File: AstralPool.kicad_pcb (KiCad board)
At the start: 2 copper layers, 80 x 75 mm, 25 parts, among them J1 RJ12, J2 RJ12, J3 Header, Q1 2N3904, U1 LM2678T-5.0/NOPB

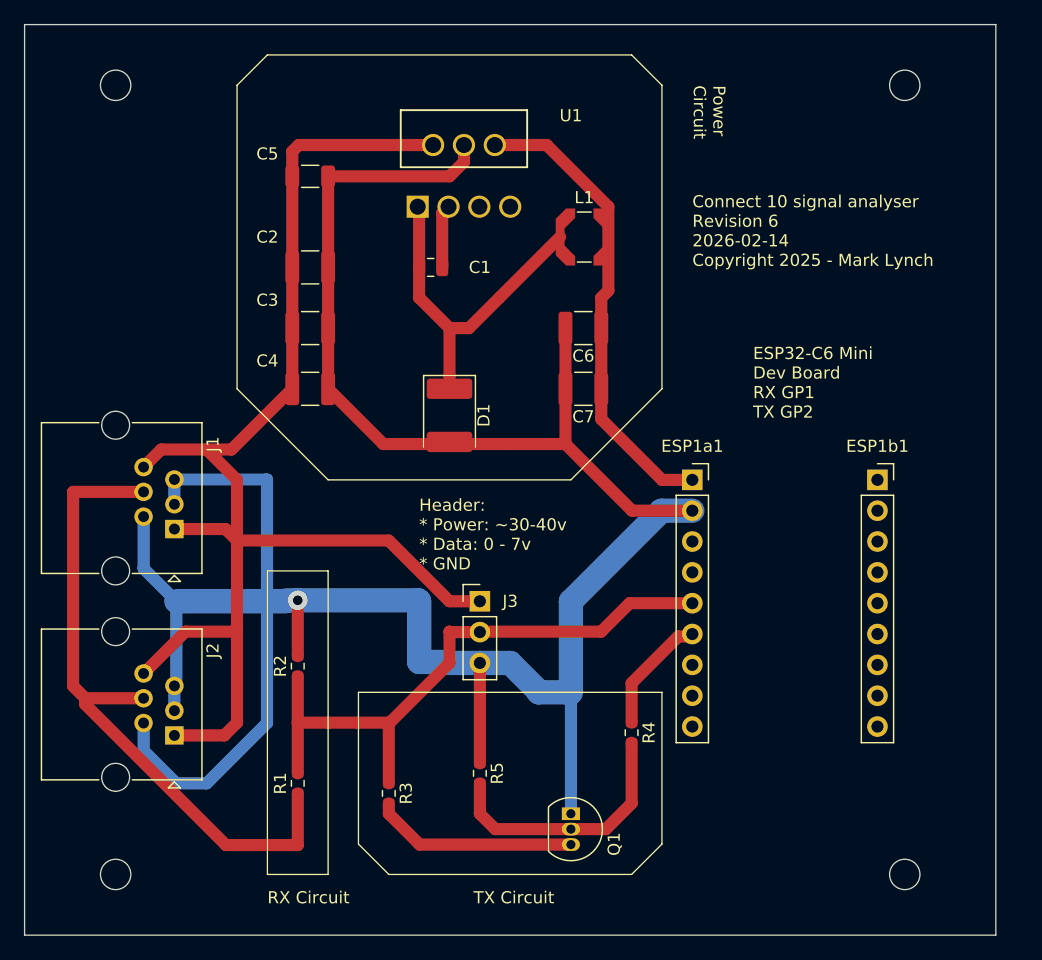
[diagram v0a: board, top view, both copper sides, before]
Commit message: ### Changed - Reorient board to allow all plugs on one side
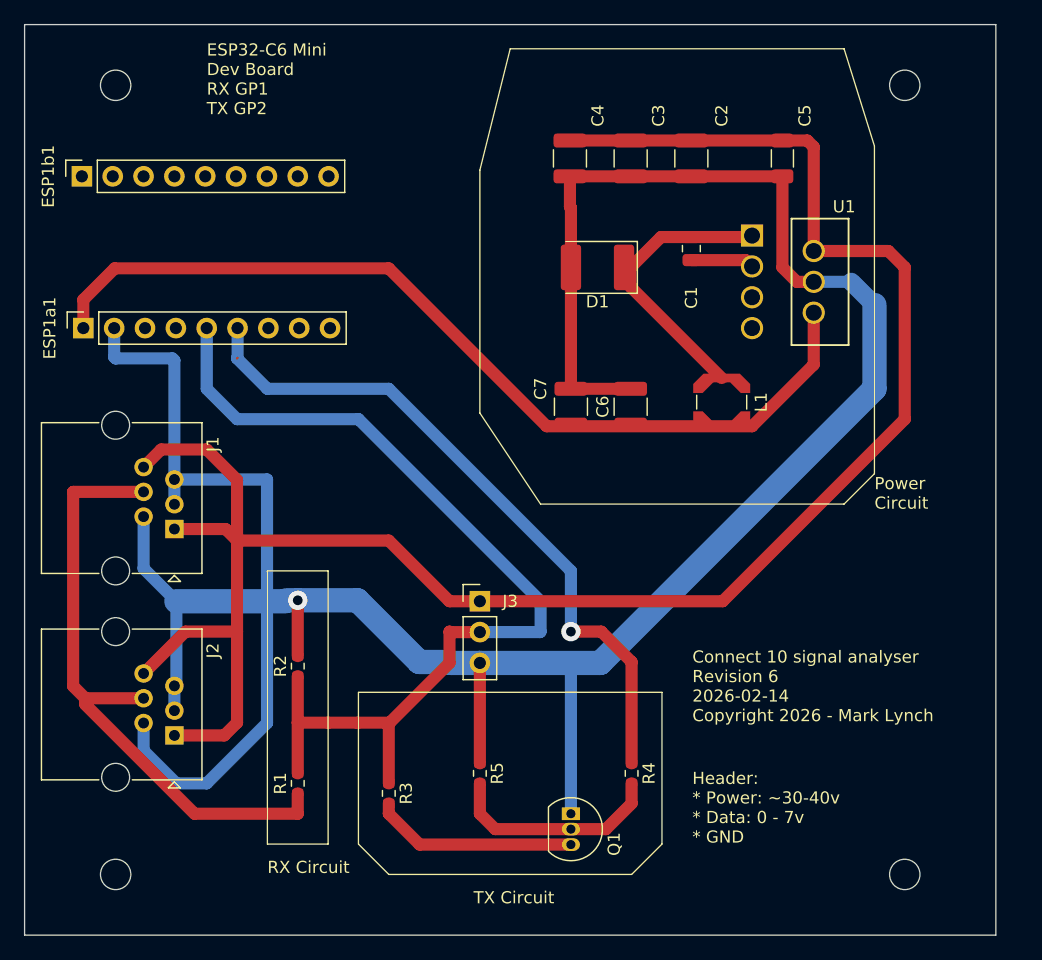
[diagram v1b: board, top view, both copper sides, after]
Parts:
- REF** (x4): value MountingHole_2.5mm -> Mounting 2.5mm
- moved ESP1b1 70.1 mm to (59.7, 35.0), turned to 90 degrees
- moved ESP1a1 51.7 mm to (59.8, 47.5), turned to 90 degrees
- moved C5 38.9 mm to (117.4, 33.5), turned to -90 degrees
- moved U1 37.7 mm to (126.1, 47.5), turned to -90 degrees
- moved C2 32.7 mm to (109.9, 33.5), turned to -90 degrees
- moved C3 29.9 mm to (104.9, 33.5), turned to -90 degrees
- moved C4 28.6 mm to (99.9, 33.5), turned to -90 degrees
- moved C1 21.5 mm to (109.9, 41.0), turned to -90 degrees
- moved L1 17.7 mm to (112.4, 53.6), turned to -90 degrees
- moved D1 17.2 mm to (102.2, 42.5), turned to 180 degrees
- moved C6 7.56 mm to (104.9, 54.0), turned to 90 degrees
- moved R4 3.35 mm to (105.0, 84.2)
- moved C7 1.80 mm to (100.0, 54.0), turned to 90 degrees
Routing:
- net +24V (from connector): track 112.2 -> 162.3 mm
- net Net-(ESP1a1-Pin_6): track 9.93 -> 56.7 mm, vias 0 -> 1
- net +5V (from buck power): track 38.8 -> 75.3 mm
- net Net-(ESP1a1-Pin_5): track 51.2 -> 80.0 mm
- net GND (from connector): track 218.9 -> 237.2 mm
- net Net-(D1-K): track 28.3 -> 23.3 mm
- net Net-(J1-Pad4): track 55.1 -> 51.4 mm
- net Net-(Q1-B): track 21.4 -> 18.1 mm

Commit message: ### Changed - Rev 7 - Reorient power circuit again to make cleaner
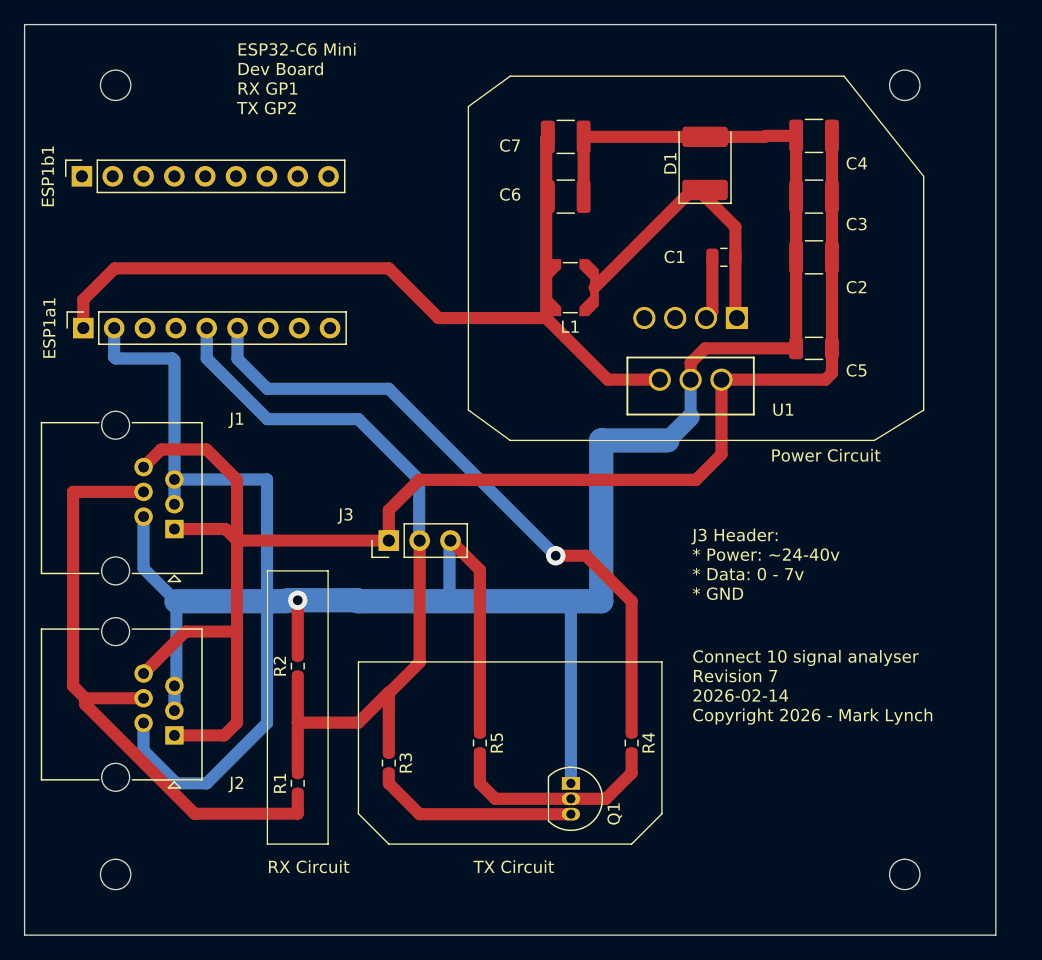
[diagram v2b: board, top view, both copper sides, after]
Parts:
- moved U1 22.6 mm to (106.0, 57.9), turned to 180 degrees
- moved C7 22.2 mm to (99.6, 31.8), turned to 0 degrees
- moved C4 20.2 mm to (120.0, 31.7), turned to 180 degrees
- moved C6 18.1 mm to (99.6, 36.7), turned to 0 degrees
- moved C5 15.9 mm to (120.0, 49.2), turned to 180 degrees
- moved L1 15.6 mm to (100.0, 44.2), turned to 180 degrees
- moved C3 15.4 mm to (120.0, 36.7), turned to 180 degrees
- moved C2 13.0 mm to (120.0, 41.7), turned to 180 degrees
- moved D1 12.3 mm to (111.0, 33.9), turned to 90 degrees
- moved J3 9.01 mm to (85.0, 65.0), turned to 90 degrees
- moved C1 2.78 mm to (112.6, 41.7), turned to 180 degrees
- moved Q1 2.50 mm to (100.0, 85.0)
- moved R3 2.50 mm to (85.0, 83.3)
- moved R4 2.50 mm to (105.0, 81.7)
- moved R5 2.50 mm to (92.5, 81.7)
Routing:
- net +24V (from connector): track 162.3 -> 128.9 mm
- net Net-(ESP1a1-Pin_5): track 80.0 -> 64.3 mm
- net GND (from connector): track 237.2 -> 231.2 mm
- net +5V (from buck power): track 75.3 -> 69.7 mm
- net Net-(ESP1a1-Pin_6): track 56.7 -> 54.1 mm
- net Net-(D1-K): track 23.3 -> 24.1 mm
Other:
- board text added: "J3 Header: * Power: ~24-40v * Data: 0 - 7v * GND"
- board text removed: "Header: * Power: ~30-40v * Data: 0 - 7v * GND"

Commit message: ### Added - Reworked and tested TX circuit
### Changed
- Rev 8 - Updated all footprints to correct specs
- Rev 8 - Updated components to include part numbers
- Rev 8 - Respecced the power circuit based on TI toolins
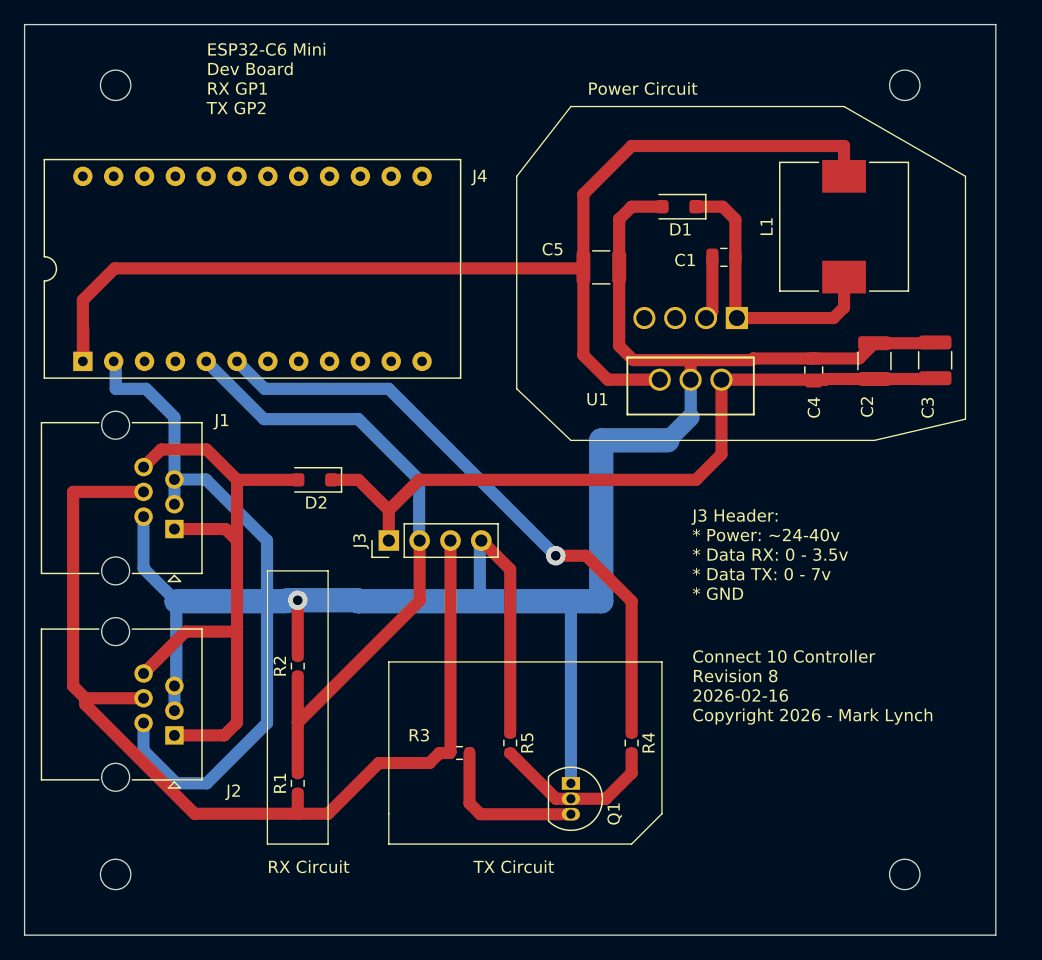
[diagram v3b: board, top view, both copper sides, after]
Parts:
- removed the C4 at (120.0, 31.7)
- removed C7: C 180uF/16v, Capacitor_SMD:C_1210_3225Metric
- removed ESP1a1, ESP1b1: Conn_01x09_Socket, Connector_PinSocket_2.54mm:PinSocket_1x09_P2.54mm_Vertical
- added D2: D 6TQ045S, Diode_SMD:D_SOD-123F, F.Cu at (78.9, 60.0)
- added J4: Conn_02x12_Counter_Clockwise, Package_DIP:DIP-24_18.0mmx34.29mm_W15.24mm_Socket, F.Cu at (59.8, 50.2)
- C1: value 0.01uF -> 10nF
- C2, C3: value C 15uF/50v -> C 10uF/63v
- C4: renamed from C5; value 0.47uF -> 100nF/50v; footprint Capacitor_SMD:C_1206_3216Metric -> Capacitor_SMD:C_0805_2012Metric
- C5: renamed from C6; value C 180uF/16v -> C 47uF/16v
- D1: footprint Diode_SMD:D_2114_3652Metric -> Diode_SMD:D_SOD-123F
- J3: footprint Connector_PinHeader_2.54mm:PinHeader_1x03_P2.54mm_Vertical -> Connector_PinHeader_2.54mm:PinHeader_1x04_P2.54mm_Vertical
- L1: value L 22uH -> L 120uH; footprint Inductor_SMD:L_Coilcraft_LPS4414 -> Inductor_SMD:L_10.4x10.4_H4.8
- R1, R2: value R220k -> R100k
- moved L1 23.1 mm to (122.5, 39.1), turned to 90 degrees
- moved C3 16.8 mm to (130.0, 50.2), turned to 90 degrees
- moved C2 9.89 mm to (125.0, 50.2), turned to 90 degrees
- moved C5 6.52 mm to (102.5, 42.5)
- moved R3 5.88 mm to (90.8, 82.5), turned to 0 degrees
- moved D1 4.16 mm to (108.9, 37.5), turned to 180 degrees
- moved R5 2.50 mm to (95.0, 81.7)
- moved C4 1.78 mm to (120.0, 51.0), turned to 90 degrees
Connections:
- C2 pad 1: +24V (from connector) -> Net-(D2-K)
- C3 pad 1: +24V (from connector) -> Net-(D2-K)
- C4 pad 1: +24V (from connector) -> Net-(D2-K)
- J1 pad 4: Net-(J1-Pad4) -> Net-(J3-Pin_3)
- J2 pad 4: Net-(J1-Pad4) -> Net-(J3-Pin_3)
- J3 pad 1: +24V (from connector) -> Net-(D2-K)
- J3 pad 2: Net-(ESP1a1-Pin_5) -> Net-(J3-Pin_2)
- J3 pad 3: GND (from connector) -> Net-(J3-Pin_3)
- R1 pad 1: Net-(J1-Pad4) -> Net-(J3-Pin_3)
- R1 pad 2: Net-(ESP1a1-Pin_5) -> Net-(J3-Pin_2)
- R2 pad 1: Net-(ESP1a1-Pin_5) -> Net-(J3-Pin_2)
- R3 pad 1: Net-(ESP1a1-Pin_5) -> Net-(J3-Pin_3)
- U1 pad 2: +24V (from connector) -> Net-(D2-K)
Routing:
- net Net-(J3-Pin_3): track 0.00 -> 83.5 mm
- net +24V (from connector): track 128.9 -> 54.6 mm
- net Net-(ESP1a1-Pin_5): track 64.3 -> 0.00 mm
- net Net-(D2-K): track 0.00 -> 61.3 mm
- net Net-(J3-Pin_2): track 0.00 -> 53.8 mm
- net Net-(J1-Pad4): track 51.4 -> 0.00 mm
- net +5V (from buck power): track 69.7 -> 96.1 mm
- net GND (from connector): track 231.2 -> 217.0 mm
- net Net-(Q1-C): track 16.9 -> 12.9 mm
- net Net-(Q1-B): track 18.1 -> 14.1 mm
- net Net-(J4-Pin_6): track 54.1 -> 51.5 mm
- net Net-(D1-K): track 24.1 -> 23.5 mm
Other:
- board text added: "J3 Header: * Power: ~24-40v * Data RX: 0 - 3.5v * Data TX: 0 - 7v * GND"
- board text removed: "J3 Header: * Power: ~24-40v * Data: 0 - 7v * GND"
